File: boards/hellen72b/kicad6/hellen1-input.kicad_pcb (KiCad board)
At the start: 2 copper layers, 30.9 x 14.6 mm, 57 parts, among them M200 Hellen One : Input Module int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, P200 Vref1, P201 Vref2

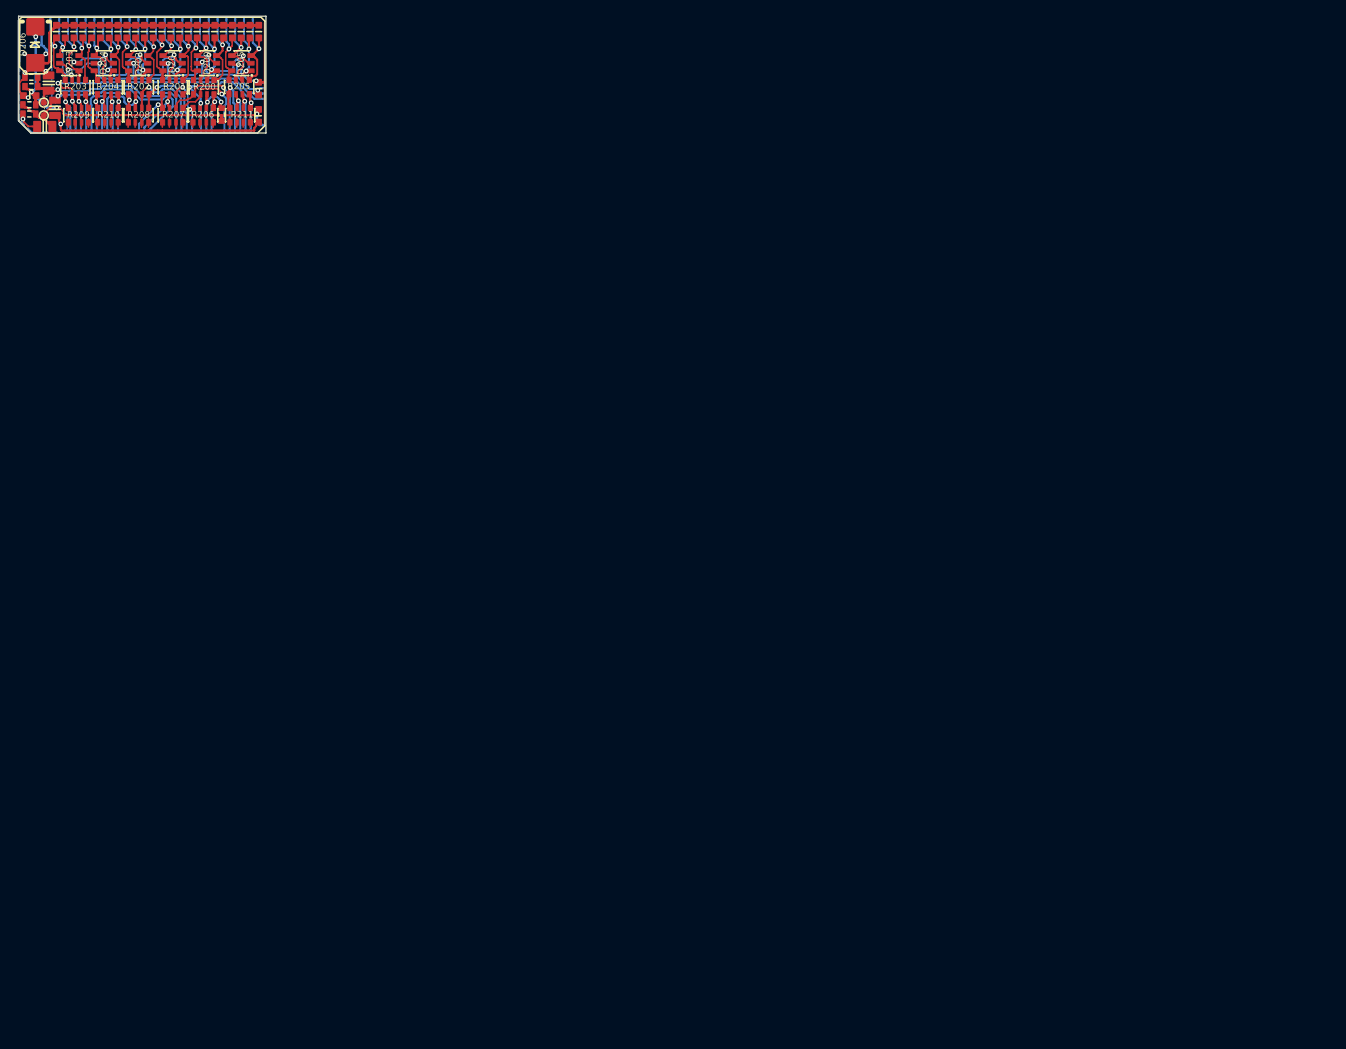
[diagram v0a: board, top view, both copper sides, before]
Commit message: update exported kicad files after refactoring
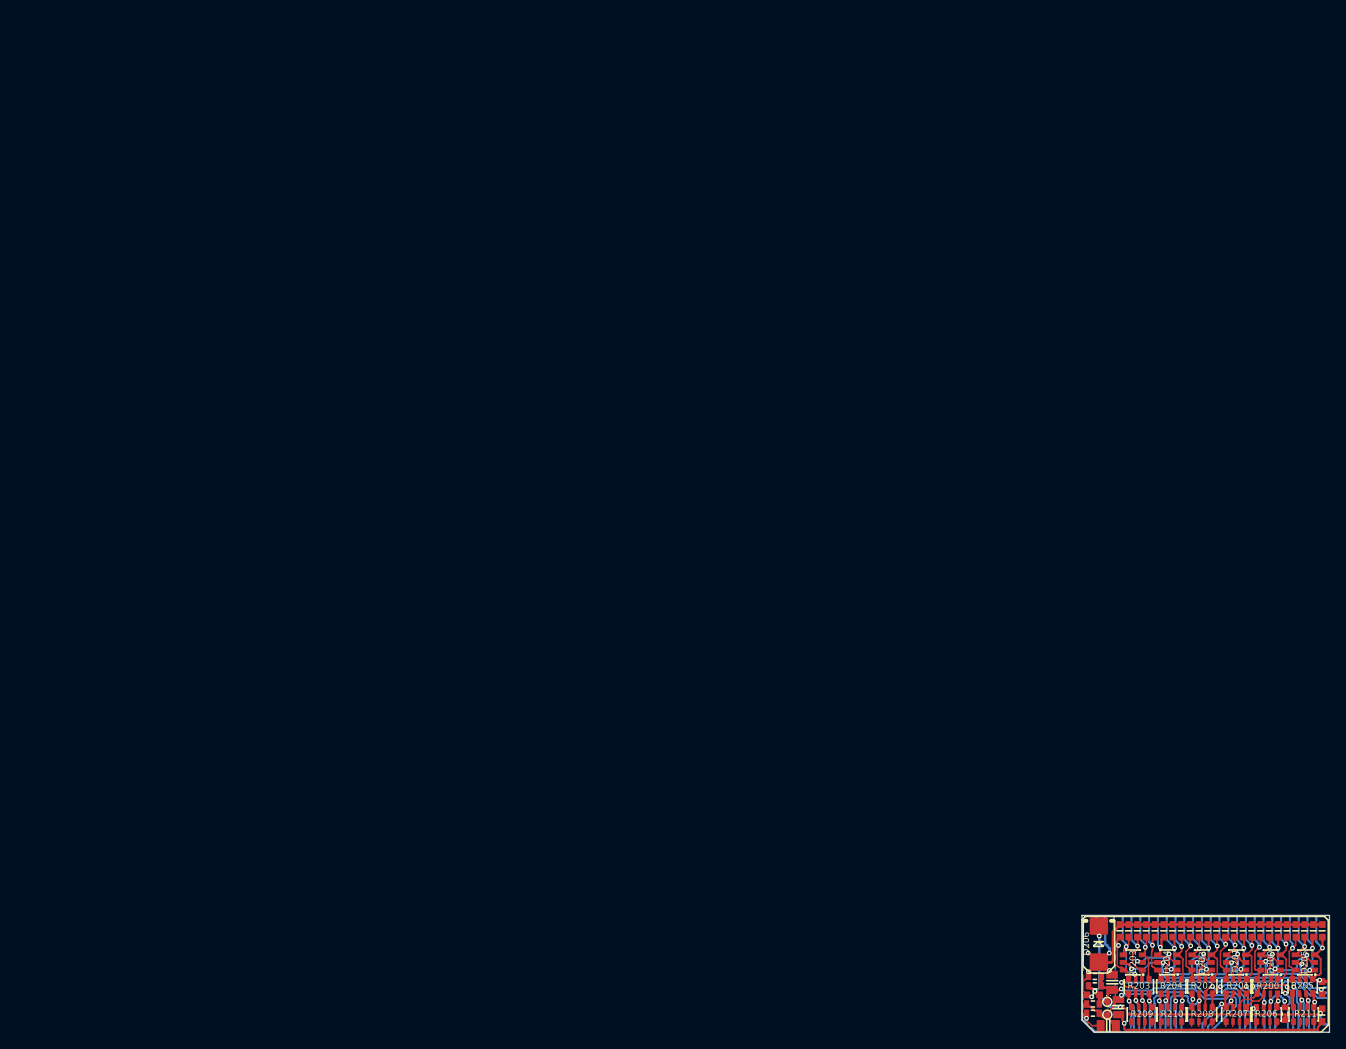
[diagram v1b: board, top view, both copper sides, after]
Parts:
- M200: value Hellen One : Input Module interface -> Module:input/0.1
- moved P201 174.1 mm to (136.2, 108.5)
- moved C201 174.1 mm to (156.5, 99.6)
- moved C202 174.1 mm to (157.6, 99.6)
- moved C203 174.1 mm to (158.7, 99.6)
- moved C204 174.1 mm to (151.0, 99.6)
- moved C205 174.1 mm to (152.1, 99.6)
- moved C206 174.1 mm to (153.2, 99.6)
- moved C208 174.1 mm to (146.6, 99.6)
- moved C209 174.1 mm to (147.7, 99.6)
- moved C211 174.1 mm to (149.9, 99.6)
- moved C214 174.1 mm to (140.0, 99.6)
- moved C215 174.1 mm to (141.1, 99.6)
- moved C216 174.1 mm to (142.2, 99.6)
- moved C218 174.1 mm to (144.4, 99.6)
- moved C219 174.1 mm to (145.5, 99.6)
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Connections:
- net IN_MAP4 renamed IN_RES3
- net MAP4 renamed RES3
- net PULL_MAP4 renamed PULL_RES3
- M200 pad E5: GND -> V5A
